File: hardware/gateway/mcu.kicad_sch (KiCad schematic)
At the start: 31 parts, among them IC1 STM8L151K4T6, IC5 MB85RC64TAPNF-G-BDERE1, J1 G8250041000YEU, J2 M20-9770342, Q1 IRLML6402TRPBF, U1 2462

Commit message: EG-11 ERC passed.
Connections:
- net GND: no longer IC1.25 (PC0), IC1.26 (PC1), IC5.5 (SDA), IC5.6 (SCL), R11.1, R12.1
- new net SCL: IC1.26 (PC1), IC5.6 (SCL), R11.1
- new net SDA: IC1.25 (PC0), IC5.5 (SDA), R12.1
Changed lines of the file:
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@@
 	)
 	(junction
+		(at 128.27 22.86)
+		(diameter 0)
+		(color 0 0 0 0)
+	)
+	(junction
 		(at 49.53 27.94)
 		(diameter 0)
@@
 	(wire
 		(pts
+			(xy 119.38 22.86) (xy 128.27 22.86)
+		)
+		(stroke
+			(width 0)
+			(type default)
+		)
+	)
+	(wire
+		(pts
 			(xy 58.42 25.4) (xy 66.04 25.4)
 		)
@@
 	(wire
 		(pts
+			(xy 119.38 19.05) (xy 119.38 22.86)
+		)
+		(stroke
+			(width 0)
+			(type default)
+		)
+	)
+	(wire
+		(pts
 			(xy 71.12 134.62) (xy 78.74 134.62)
 		)
@@
 	(wire
 		(pts
-			(xy 210.82 135.89) (xy 210.82 147.32)
-		)
-		(stroke
-			(width 0)
-			(type default)
-		)
-	)
-	(wire
-		(pts
 			(xy 86.36 22.86) (xy 91.44 22.86)
 		)
@@
 	(wire
 		(pts
-			(xy 201.93 133.35) (xy 201.93 147.32)
-		)
-		(stroke
-			(width 0)
-			(type default)
-		)
-	)
-	(wire
-		(pts
 			(xy 69.85 73.66) (xy 81.28 73.66)
 		)
@@
 	)
 	(symbol
+		(lib_id "power:PWR_FLAG")
+		(at 119.38 19.05 0)
+		(unit 1)
+		(exclude_from_sim no)
+		(in_bom yes)
+		(on_board yes)
+		(dnp no)
+		(fields_autoplaced yes)
+		(property "Reference" "#FLG03"
+			(at 119.38 17.145 0)
+			(effects
+				(font
+					(size 1.27 1.27)
+				)
+				(hide yes)
+			)
+		)
+		(property "Value" "PWR_FLAG"
+			(at 119.38 13.97 0)
+			(effects
+				(font
+					(size 1.27 1.27)
+				)
+			)
+		)
+		(property "Footprint" ""
+			(at 119.38 19.05 0)
+			(effects
+				(font
+					(size 1.27 1.27)
+				)
+				(hide yes)
+			)
+		)
+		(property "Datasheet" "~"
+			(at 119.38 19.05 0)
+			(effects
+				(font
+					(size 1.27 1.27)
+				)
+				(hide yes)
+			)
+		)
+		(property "Description" "Special symbol for telling ERC where power comes from"
+			(at 119.38 19.05 0)
+			(effects
+				(font
+					(size 1.27 1.27)
+				)
+				(hide yes)
+			)
+		)
+		(pin "1"
+		)
+		(instances
+			(project "gateway"
+				(path "/d3cb7130-decc-418b-958e-e5d84a8d867f/ec220677-d66d-4ee1-961f-1c93fb46783a"
+					(reference "#FLG03")
+					(unit 1)
+				)
+			)
+		)
+	)
+	(symbol
 		(lib_id "Device:C")
 		(at 29.21 154.94 0)
@@
 	(symbol
 		(lib_id "power:GND")
-		(at 201.93 147.32 0)
-		(unit 1)
-		(exclude_from_sim no)
-		(in_bom yes)
-		(on_board yes)
-		(dnp no)
-		(fields_autoplaced yes)
-		(property "Reference" "#PWR058"
-			(at 201.93 153.67 0)
-			(effects
-				(font
-					(size 1.27 1.27)
-				)
-				(hide yes)
-			)
-		)
-		(property "Value" "GND"
-			(at 201.93 152.4 0)
-			(effects
-				(font
-					(size 1.27 1.27)
-				)
-			)
-		)
-		(property "Footprint" ""
-			(at 201.93 147.32 0)
-			(effects
-				(font
-					(size 1.27 1.27)
-				)
-				(hide yes)
-			)
-		)
-		(property "Datasheet" ""
-			(at 201.93 147.32 0)
-			(effects
-				(font
-					(size 1.27 1.27)
-				)
-				(hide yes)
-			)
-		)
-		(property "Description" "Power symbol creates a global label with name \"GND\" , ground"
-			(at 201.93 147.32 0)
-			(effects
-				(font
-					(size 1.27 1.27)
-				)
-				(hide yes)
-			)
-		)
-		(pin "1"
-		)
-		(instances
-			(project "gateway"
-				(path "/d3cb7130-decc-418b-958e-e5d84a8d867f/ec220677-d66d-4ee1-961f-1c93fb46783a"
-					(reference "#PWR058")
-					(unit 1)
-				)
-			)
-		)
-	)
-	(symbol
-		(lib_id "power:GND")
 		(at 156.21 147.32 0)
 		(unit 1)
@@
 					(unit 1)
 				)
-			)
-		)
-	)
-	(symbol
-		(lib_id "power:GND")
-		(at 210.82 147.32 0)
-		(unit 1)
-		(exclude_from_sim no)
-		(in_bom yes)
-		(on_board yes)
-		(dnp no)
-		(fields_autoplaced yes)
-		(property "Reference" "#PWR059"
-			(at 210.82 153.67 0)
-			(effects
-				(font
-					(size 1.27 1.27)
-				)
-				(hide yes)
-			)
-		)
-		(property "Value" "GND"
-			(at 210.82 152.4 0)
-			(effects
-				(font
-					(size 1.27 1.27)
-				)
-			)
-		)
-		(property "Footprint" ""
-			(at 210.82 147.32 0)
-			(effects
-				(font
-					(size 1.27 1.27)
-				)
-				(hide yes)
-			)
-		)
-		(property "Datasheet" ""
-			(at 210.82 147.32 0)
-			(effects
-				(font
-					(size 1.27 1.27)
-				)
-				(hide yes)
-			)
-		)
-		(property "Description" "Power symbol creates a global label with name \"GND\" , ground"
-			(at 210.82 147.32 0)
-			(effects
-				(font
-					(size 1.27 1.27)
-				)
-				(hide yes)
-			)
-		)
-		(pin "1"
-		)
-		(instances
-			(project "gateway"
-				(path "/d3cb7130-decc-418b-958e-e5d84a8d867f/ec220677-d66d-4ee1-961f-1c93fb46783a"
-					(reference "#PWR059")
-					(unit 1)
-				)

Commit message: EG-12 All components placed. RF connected, except antenna. Buzzer connected, buzzer power supply connected, FRAM connected. Majority os MCU connections  missing.
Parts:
- C1, C2, C5, C8: footprint Capacitor_SMD:C_0603_1608Metric -> Capacitor_SMD:C_0402_1005Metric; Manufacturer_Name Murata -> Yageo; Manufacturer_Part_Number GCJ188R72A104KA1D -> CC0402KRX7R7BB104; Mouser Part Number 81-GCJ188R72A104KA1D -> 603-CC402KRX7R7BB104; Mouser Price/Stock https://pt.mouser.com/ProductDetail/Murata-Electronics/GCJ1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 -> https://pt.mouser.com/ProductDetail/YAGEO/CC0402KRX7R7BB104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
- C4, C7: footprint Capacitor_SMD:C_0603_1608Metric -> Capacitor_SMD:C_0402_1005Metric; Manufacturer_Name TAYO YUDEN -> Murata; Manufacturer_Part_Number MBASE168SB7105KTNA18 -> GXT155R60J105KE01D; Mouser Part Number 963-MBASE168SB7105KT -> 81-GXT155R60J105KE1D; Mouser Price/Stock https://pt.mouser.com/ProductDetail/TAIYO-YUDEN/MBASE168SB7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 -> https://pt.mouser.com/ProductDetail/Murata-Electronics/GXT1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

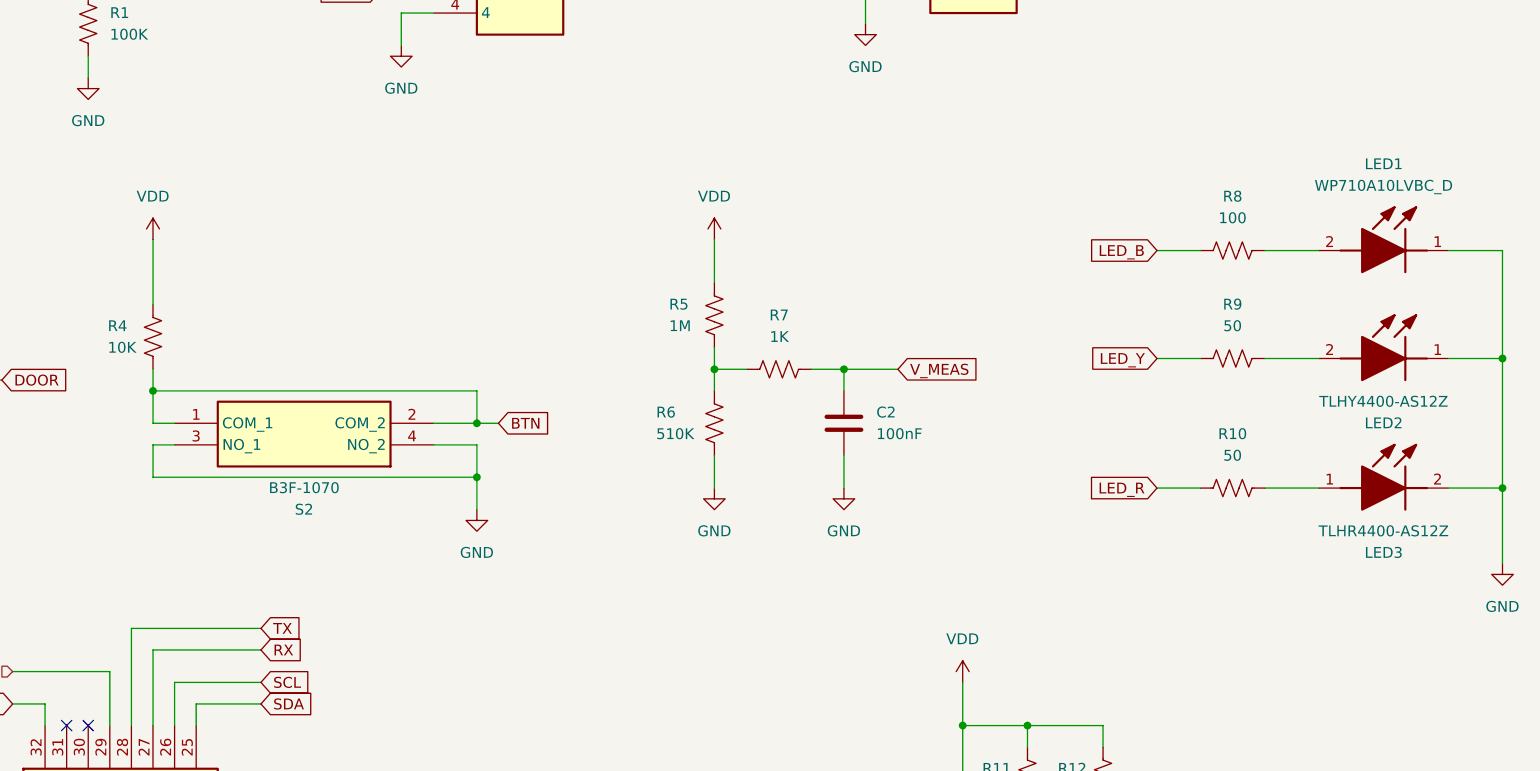
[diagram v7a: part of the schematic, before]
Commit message: EG-12 All components connected, except antenna and ground plane.
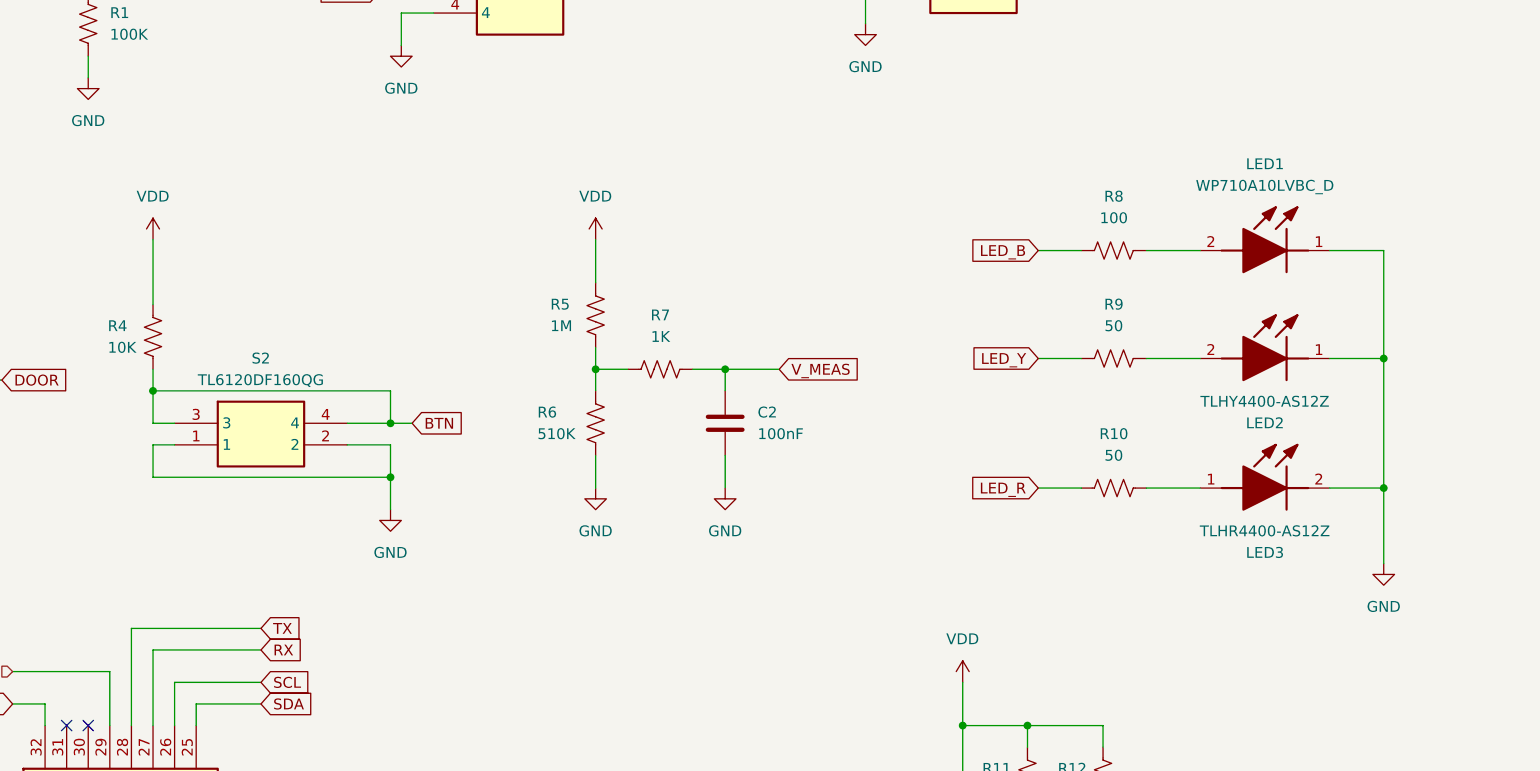
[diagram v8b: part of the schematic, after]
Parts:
- removed S2: B3F-1070, MyParts:B3F1060, symbol B3F-1070:B3F-1070
- added S2: TL6120DF160QG, MyParts:TL6120DF160QG, symbol TL6120DF160QG:TL6120DF160QG
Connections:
- net BTN: now also S2.3, S2.4
- net GND: now also S2.1, S2.2
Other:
- moved on the sheet: C2, LED1, LED2, LED3, R10, R5, R6, R7, R8, R9
